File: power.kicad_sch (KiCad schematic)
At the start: 9 parts

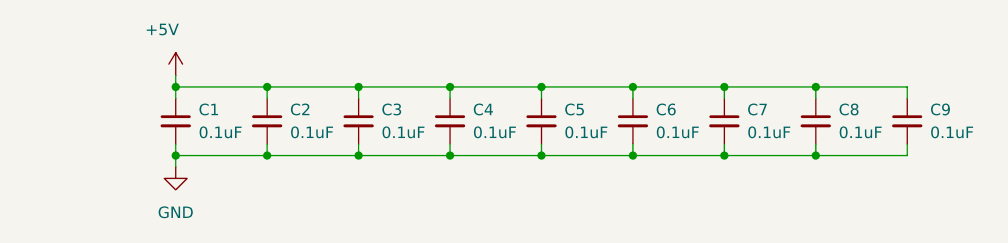
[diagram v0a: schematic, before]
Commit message: Update Schematic for card edge connector
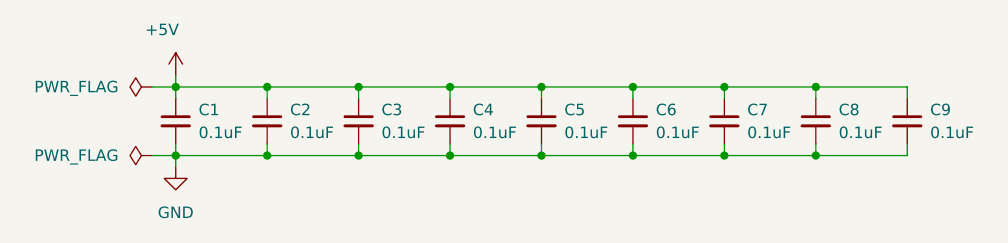
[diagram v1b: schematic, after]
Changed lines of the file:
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@@
+	(wire
+		(pts
+			(xy 60.96 92.71) (xy 63.5 92.71)
+		)
+		(stroke
+			(width 0)
+			(type default)
+		)
+	)
+	(wire
+		(pts
+			(xy 60.96 85.09) (xy 63.5 85.09)
+		)
+		(stroke
+			(width 0)
+			(type default)
+		)
+	)
 	(wire
 		(pts
@@
 			(width 0)
 			(type default)
+		)
+	)
+	(symbol
+		(lib_id "power:PWR_FLAG")
+		(at 60.96 92.71 90)
+		(unit 1)
+		(body_style 1)
+		(exclude_from_sim no)
+		(in_bom yes)
+		(on_board yes)
+		(in_pos_files yes)
+		(dnp no)
+		(fields_autoplaced yes)
+		(property "Reference" "#FLG02"
+			(at 59.055 92.71 0)
+			(hide yes)
+			(show_name no)
+			(do_not_autoplace no)
+			(effects
+				(font
+					(size 1.27 1.27)
+				)
+			)
+		)
+		(property "Value" "PWR_FLAG"
+			(at 57.15 92.7099 90)
+			(show_name no)
+			(do_not_autoplace no)
+			(effects
+				(font
+					(size 1.27 1.27)
+				)
+				(justify left)
+			)
+		)
+		(property "Footprint" ""
+			(at 60.96 92.71 0)
+			(hide yes)
+			(show_name no)
+			(do_not_autoplace no)
+			(effects
+				(font
+					(size 1.27 1.27)
+				)
+			)
+		)
+		(property "Datasheet" ""
+			(at 60.96 92.71 0)
+			(hide yes)
+			(show_name no)
+			(do_not_autoplace no)
+			(effects
+				(font
+					(size 1.27 1.27)
+				)
+			)
+		)
+		(property "Description" "Special symbol for telling ERC where power comes from"
+			(at 60.96 92.71 0)
+			(hide yes)
+			(show_name no)
+			(do_not_autoplace no)
+			(effects
+				(font
+					(size 1.27 1.27)
+				)
+			)
+		)
+		(pin "1"
+		)
+		(instances
+			(project "AmigaA1000RAM"
+				(path "/ae88afc5-9dfe-4e8c-91a0-a4895e2c581d/01d35853-1123-4b64-b51d-30d7509a333e"
+					(reference "#FLG02")
+					(unit 1)
+				)
+			)
 		)
 	)
@@
 					(unit 1)
 				)
+			)
+		)
+	)
+	(symbol
+		(lib_id "power:PWR_FLAG")
+		(at 60.96 85.09 90)
+		(unit 1)
+		(body_style 1)
+		(exclude_from_sim no)
+		(in_bom yes)
+		(on_board yes)
+		(in_pos_files yes)
+		(dnp no)
+		(fields_autoplaced yes)
+		(property "Reference" "#FLG01"
+			(at 59.055 85.09 0)
+			(hide yes)
+			(show_name no)
+			(do_not_autoplace no)
+			(effects
+				(font
+					(size 1.27 1.27)
+				)
+			)
+		)
+		(property "Value" "PWR_FLAG"
+			(at 57.15 85.0899 90)
+			(show_name no)
+			(do_not_autoplace no)
+			(effects
+				(font
+					(size 1.27 1.27)
+				)
+				(justify left)
+			)
+		)
+		(property "Footprint" ""
+			(at 60.96 85.09 0)
+			(hide yes)
+			(show_name no)
+			(do_not_autoplace no)
+			(effects
+				(font
+					(size 1.27 1.27)
+				)
+			)
+		)
+		(property "Datasheet" ""
+			(at 60.96 85.09 0)
+			(hide yes)
+			(show_name no)
+			(do_not_autoplace no)
+			(effects
+				(font
+					(size 1.27 1.27)
+				)
+			)
+		)
+		(property "Description" "Special symbol for telling ERC where power comes from"
+			(at 60.96 85.09 0)
+			(hide yes)
+			(show_name no)
+			(do_not_autoplace no)
+			(effects
+				(font
+					(size 1.27 1.27)
+				)
+			)
+		)
+		(pin "1"
+		)
+		(instances
+			(project "AmigaA1000RAM"
+				(path "/ae88afc5-9dfe-4e8c-91a0-a4895e2c581d/01d35853-1123-4b64-b51d-30d7509a333e"
+					(reference "#FLG01")
+					(unit 1)
+				)
